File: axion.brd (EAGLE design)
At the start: 100 x 80.5 mm, 148 parts, among them IC1 3.3V, IC2 5V, Q2 12.288Mhz, U10 MIC2039, U11 WM8731, U2 Intel Edison, U4 FT232RLSSOP, U5 PCA9306D, U6 74HC4050, U7 TPA2005D1DGN, X2 ZX62R-AB-5P, X3 ST-005-G, X4 ZX62R-B-5P

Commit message: Power microSD
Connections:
- removed net N$49: JP25.4
- removed net N$51: JP25.6
- net +3V3: now also JP25.4
- net DGND: now also JP25.6
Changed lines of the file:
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@@
 <element name="U5" library="NXP_By_element14_Batch_1" package="SOIC127P600X175-8N" value="PCA9306D" x="66.7381" y="34.2527" smashed="yes" rot="MR90">
 <attribute name="MPN" value="PCA9306D,118" x="66.7381" y="34.2527" size="1.778" layer="28" rot="MR90" display="off"/>
+<attribute name="NAME" x="71.28978125" y="32.0683" size="1.016" layer="26" ratio="10" rot="SMR90"/>
+<attribute name="OC_FARNELL" value="1831194" x="66.7381" y="34.2527" size="1.778" layer="28" rot="MR90" display="off"/>
 <attribute name="OC_NEWARK" value="70R6428" x="66.7381" y="34.2527" size="1.778" layer="28" rot="MR90" display="off"/>
+<attribute name="PACKAGE" value="SOIC-8" x="66.7381" y="34.2527" size="1.778" layer="28" rot="MR90" display="off"/>
 <attribute name="SUPPLIER" value="NXP" x="66.7381" y="34.2527" size="1.778" layer="28" rot="MR90" display="off"/>
-<attribute name="OC_FARNELL" value="1831194" x="66.7381" y="34.2527" size="1.778" layer="28" rot="MR90" display="off"/>
-<attribute name="PACKAGE" value="SOIC-8" x="66.7381" y="34.2527" size="1.778" layer="28" rot="MR90" display="off"/>
-<attribute name="NAME" x="71.28978125" y="32.0683" size="1.016" layer="26" ratio="10" rot="SMR90"/>
 <attribute name="VALUE" x="70.062959375" y="31.923521875" size="0.8128" layer="28" ratio="10" rot="SMR90"/>
 </element>
@@
 </element>
 <element name="Q2" library="adafruit" package="HC49/S" value="12.288Mhz" x="35.6235" y="66.4972" rot="R90">
+<attribute name="MF" value="" x="35.6235" y="66.4972" size="1.778" layer="27" rot="R90" display="off"/>
+<attribute name="MPN" value="" x="35.6235" y="66.4972" size="1.778" layer="27" rot="R90" display="off"/>
 <attribute name="OC_FARNELL" value="1667008" x="35.6235" y="66.4972" size="1.778" layer="27" rot="R90" display="off"/>
 <attribute name="OC_NEWARK" value="unknown" x="35.6235" y="66.4972" size="1.778" layer="27" rot="R90" display="off"/>
-<attribute name="MF" value="" x="35.6235" y="66.4972" size="1.778" layer="27" rot="R90" display="off"/>
-<attribute name="MPN" value="" x="35.6235" y="66.4972" size="1.778" layer="27" rot="R90" display="off"/>
 </element>
 <element name="C32" library="resistor" package="C1608" value="22p" x="37.7825" y="60.0202" rot="MR0"/>
@@
 <vertex x="25.3992375" y="0"/>
 </polygon>
+<contactref element="JP25" pad="6"/>
+<wire x1="88.0872" y1="71.247" x2="83.8169" y2="74.3721" width="0" layer="19" extent="16-16"/>
 </signal>
 <signal name="+3V3" class="2">
@@
 <wire x1="55.963059375" y1="53.130196875" x2="55.8728" y2="53.22045625" width="0.1524" layer="1"/>
 <wire x1="55.8728" y1="53.22045625" x2="55.8728" y2="53.7783" width="0.1524" layer="1"/>
+<contactref element="JP25" pad="4"/>
+<wire x1="74.1697" y1="72.2217" x2="83.8169" y2="72.1721" width="0" layer="19" extent="16-16"/>
 </signal>
 <signal name="+5V" class="2">
@@
 <via x="84.8868" y="76.8096" extent="1-16" drill="0.3048"/>
 </signal>
-<signal name="N$49">
-<contactref element="JP25" pad="4"/>
-</signal>
-<signal name="N$51">
-<contactref element="JP25" pad="6"/>
-</signal>
 <signal name="N$50">

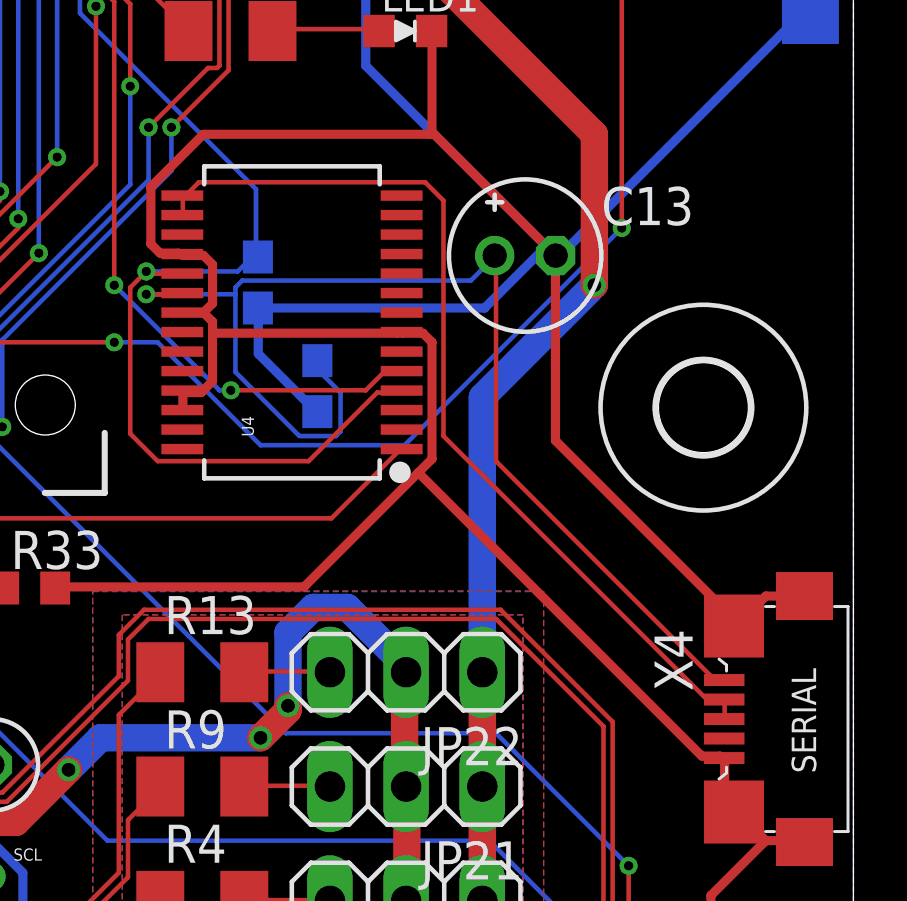
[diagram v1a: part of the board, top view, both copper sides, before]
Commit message: Disconnect between USBD{P,M} of USB-serial bridge
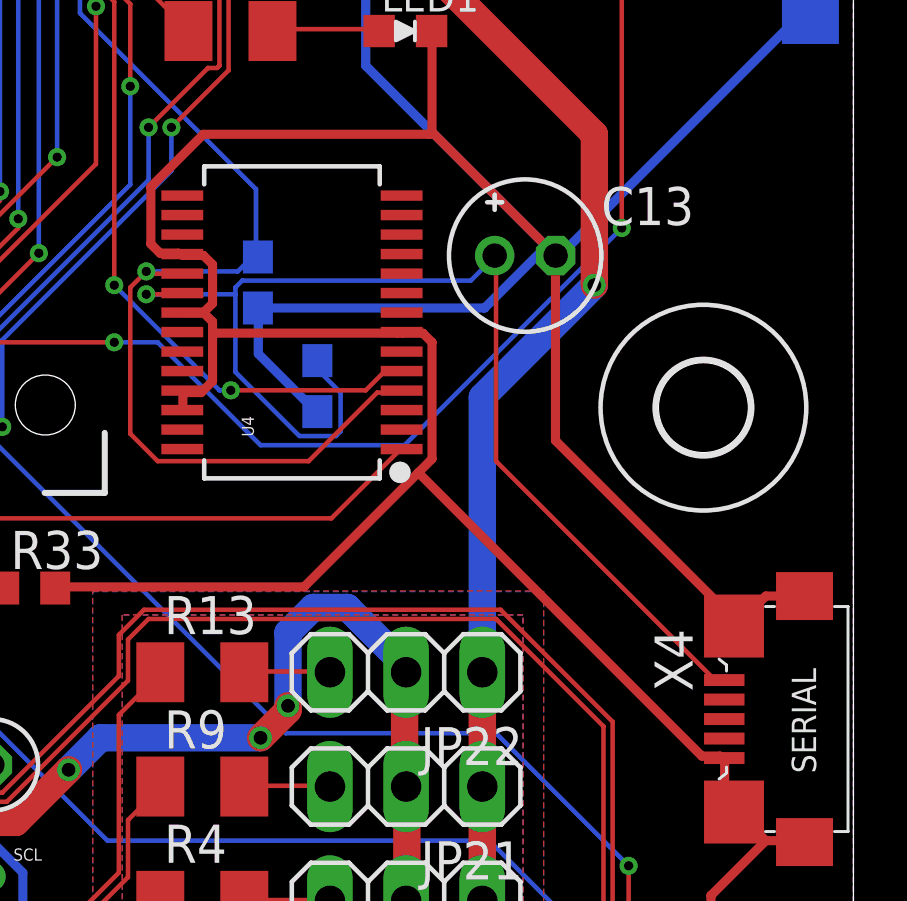
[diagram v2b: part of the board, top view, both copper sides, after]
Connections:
- new net N$49: U4.16, X4.3
- net N$8: no longer U4.16, X4.3
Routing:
- net N$8: track 31.3 -> 0.00 mm
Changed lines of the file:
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@@
 <via x="63.8556" y="50.0634" extent="1-16" drill="0.3048"/>
-</signal>
-<signal name="N$8">
-<contactref element="U4" pad="15"/>
-<contactref element="U4" pad="16"/>
-<contactref element="X4" pad="2"/>
-<contactref element="X4" pad="3"/>
-<wire x1="95.7072" y1="42.2148" x2="95.7072" y2="41.6814" width="0.1524" layer="1"/>
-<wire x1="95.7072" y1="41.6814" x2="95.695" y2="41.62" width="0.1524" layer="1"/>
-<wire x1="95.7072" y1="42.2148" x2="95.695" y2="42.27" width="0.1524" layer="1"/>
-<wire x1="77.6478" y1="59.055" x2="77.6478" y2="58.4454" width="0.1524" layer="1"/>
-<wire x1="77.6478" y1="58.4454" x2="77.6289" y2="58.4188" width="0.1524" layer="1"/>
-<wire x1="77.6478" y1="59.055" x2="77.6289" y2="59.0688" width="0.1524" layer="1"/>
-<wire x1="95.0976" y1="42.291" x2="95.631" y2="42.291" width="0.1524" layer="1"/>
-<wire x1="86.3346" y1="51.054" x2="95.0976" y2="42.291" width="0.1524" layer="1"/>
-<wire x1="86.3346" y1="58.9026" x2="86.3346" y2="51.054" width="0.1524" layer="1"/>
-<wire x1="85.725" y1="59.5122" x2="86.3346" y2="58.9026" width="0.1524" layer="1"/>
-<wire x1="78.1812" y1="59.5122" x2="85.725" y2="59.5122" width="0.1524" layer="1"/>
-<wire x1="77.724" y1="59.055" x2="78.1812" y2="59.5122" width="0.1524" layer="1"/>
-<wire x1="95.631" y1="42.291" x2="95.695" y2="42.27" width="0.1524" layer="1"/>
-<wire x1="77.724" y1="59.055" x2="77.6289" y2="59.0688" width="0.1524" layer="1"/>
 </signal>
 <signal name="I2S_RXD">
@@
 </polygon>
 </signal>
+<signal name="N$8">
+<contactref element="X4" pad="2"/>
+<contactref element="U4" pad="15"/>
+<wire x1="77.6289" y1="59.0688" x2="95.695" y2="42.27" width="0" layer="19" extent="1-1"/>
+</signal>
+<signal name="N$49">
+<contactref element="U4" pad="16"/>
+<contactref element="X4" pad="3"/>
+<wire x1="77.6289" y1="58.4188" x2="95.695" y2="41.62" width="0" layer="19" extent="1-1"/>
+</signal>
 </signals>

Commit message: Fix the order of {T,R}XD of serial
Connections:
- net UART_RXD: now also U4.1; no longer U4.5
- net UART_TXD: now also U4.5; no longer U4.1
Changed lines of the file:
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@@
 <signal name="UART_TXD">
 <contactref element="U2" pad="27"/>
-<contactref element="U4" pad="1"/>
 <wire x1="61.1124" y1="50.4444" x2="61.1124" y2="51.1302" width="0.1524" layer="1"/>
 <wire x1="63.246" y1="48.3108" x2="61.1124" y2="50.4444" width="0.1524" layer="1"/>
@@
 <wire x1="84.8868" y1="50.5968" x2="82.6008" y2="48.3108" width="0.1524" layer="1"/>
 <wire x1="61.1124" y1="51.1302" x2="61.0728" y2="51.1383" width="0.1524" layer="1"/>
-<wire x1="84.8868" y1="50.5968" x2="84.9409" y2="50.6188" width="0.1524" layer="1"/>
+<contactref element="U4" pad="5"/>
+<wire x1="84.8868" y1="50.5968" x2="84.9409" y2="53.2188" width="0" layer="19" extent="1-1"/>
 </signal>
 <signal name="UART_RXD">
 <contactref element="U2" pad="22"/>
-<contactref element="U4" pad="5"/>
 <wire x1="59.8932" y1="54.864" x2="59.8932" y2="53.7972" width="0.1524" layer="1"/>
 <wire x1="59.8932" y1="56.9976" x2="59.8932" y2="54.864" width="0.1524" layer="16"/>
@@
 <wire x1="84.8868" y1="53.1876" x2="84.3534" y2="53.1876" width="0.1524" layer="1"/>
 <wire x1="59.8932" y1="53.7972" x2="59.8728" y2="53.7783" width="0.1524" layer="1"/>
-<wire x1="84.8868" y1="53.1876" x2="84.9409" y2="53.2188" width="0.1524" layer="1"/>
 <via x="59.8932" y="54.864" extent="1-16" drill="0.3048"/>
 <via x="62.4078" y="59.2836" extent="1-16" drill="0.3048"/>
 <via x="75.3618" y="56.0832" extent="1-16" drill="0.3048"/>
 <via x="79.248" y="52.578" extent="1-16" drill="0.3048"/>
+<contactref element="U4" pad="1"/>
+<wire x1="83.7438" y1="52.578" x2="84.9409" y2="50.6188" width="0" layer="19" extent="1-1"/>
 </signal>
 <signal name="2P0">

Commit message: Fix the order of USBD{P,M} od OTG USB
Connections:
- net USB_DN: now also X2.2; no longer X2.3
- net USB_DP: now also X2.3; no longer X2.2
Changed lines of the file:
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@@
 <signal name="USB_DP">
 <contactref element="U2" pad="16"/>
-<contactref element="X2" pad="2"/>
 <wire x1="58.674" y1="54.4068" x2="58.674" y2="53.7972" width="0.1524" layer="1"/>
 <wire x1="59.6646" y1="55.3974" x2="58.674" y2="54.4068" width="0.1524" layer="1"/>
@@
 <wire x1="95.4786" y1="27.1272" x2="94.4118" y2="27.1272" width="0.1524" layer="1"/>
 <wire x1="58.674" y1="53.7972" x2="58.6728" y2="53.7783" width="0.1524" layer="1"/>
-<wire x1="95.4786" y1="27.1272" x2="95.4913" y2="27.0542" width="0.1524" layer="1"/>
 <via x="68.0466" y="56.6166" extent="1-16" drill="0.3048"/>
 <via x="92.5068" y="36.7284" extent="1-16" drill="0.3048"/>
+<contactref element="X2" pad="3"/>
+<wire x1="95.4786" y1="27.1272" x2="95.4913" y2="26.4042" width="0" layer="19" extent="1-1"/>
 </signal>
 <signal name="USB_DN">
 <contactref element="U2" pad="18"/>
-<contactref element="X2" pad="3"/>
 <wire x1="59.055" y1="53.0352" x2="59.055" y2="53.721" width="0.1524" layer="1"/>
 <wire x1="58.7502" y1="52.7304" x2="59.055" y2="53.0352" width="0.1524" layer="1"/>
@@
 <wire x1="95.4786" y1="26.4414" x2="94.6404" y2="26.4414" width="0.1524" layer="1"/>
 <wire x1="59.055" y1="53.721" x2="59.0728" y2="53.7783" width="0.1524" layer="1"/>
-<wire x1="95.4786" y1="26.4414" x2="95.4913" y2="26.4042" width="0.1524" layer="1"/>
 <via x="58.7502" y="52.7304" extent="1-16" drill="0.3048"/>
 <via x="68.961" y="41.2242" extent="1-16" drill="0.3048"/>
+<contactref element="X2" pad="2"/>
+<wire x1="95.4786" y1="26.4414" x2="95.4913" y2="27.0542" width="0" layer="19" extent="1-1"/>
 </signal>
 <signal name="USB_VBUS">

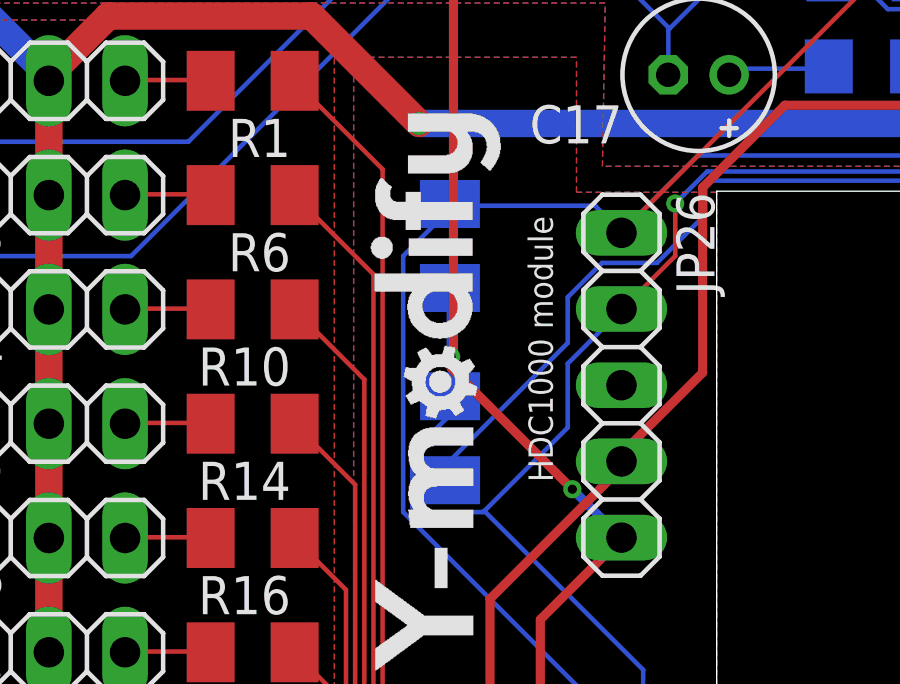
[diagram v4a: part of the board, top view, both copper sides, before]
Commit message: Remove 10k pullup of I2C
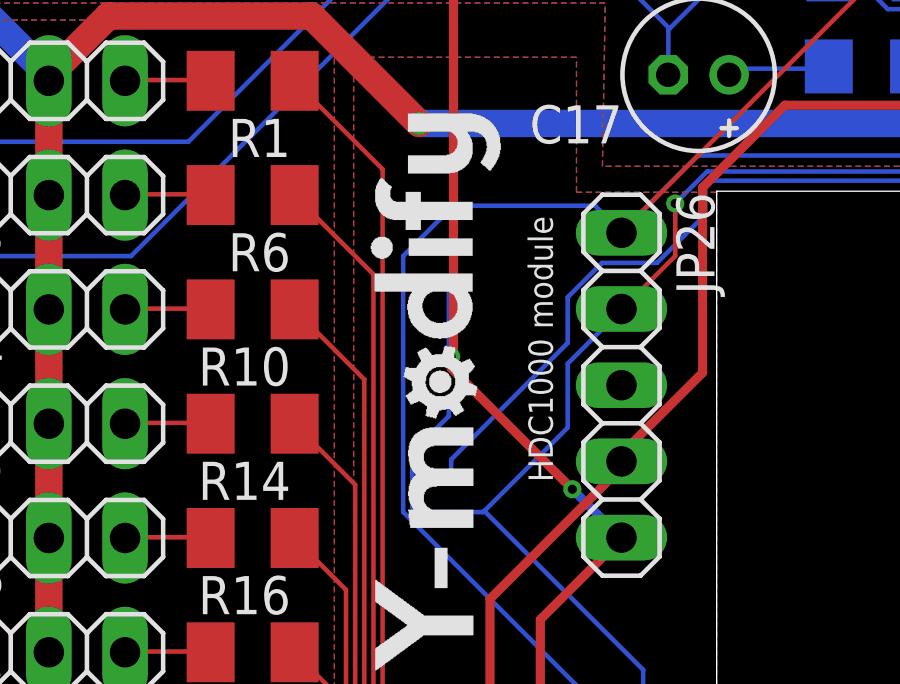
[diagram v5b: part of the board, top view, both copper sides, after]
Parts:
- removed R30, R36: 10k, resistor:M1206
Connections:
- net +3V3: no longer R30.2
- net 3V3SCL: no longer R36.1
- net 3V3SDA: no longer R30.1
- net N$10: no longer R36.2
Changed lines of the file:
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@@
 <element name="C26" library="resistor" package="E2-5" value="10u" x="25.23" y="48.78" rot="R180"/>
 <element name="R26" library="resistor" package="R0603" value="47k" x="16.09" y="55.23" rot="MR90"/>
-<element name="R30" library="resistor" package="M1206" value="10k" x="28.60801875" y="37.67328125" rot="MR270"/>
-<element name="R36" library="resistor" package="M1206" value="10k" x="28.615640625" y="31.264859375" rot="MR270"/>
 <element name="JP27" library="pinhead" package="1X02" value="PCTRL" x="61.495940625" y="78.04911875" smashed="yes" rot="R180">
 <attribute name="NAME" x="64.112140625" y="76.22031875" size="1.27" layer="25" ratio="10" rot="R180"/>
@@
 <contactref element="U11" pad="1"/>
 <contactref element="U11" pad="27"/>
-<contactref element="R30" pad="2"/>
 <contactref element="R37" pad="2"/>
 <contactref element="TP6" pad="TP"/>
@@
 <wire x1="32.6898" y1="29.5656" x2="28.6512" y2="33.6042" width="0.3048" layer="1"/>
 <wire x1="34.29" y1="27.9654" x2="32.6898" y2="29.5656" width="0.3048" layer="16"/>
-<wire x1="28.6512" y1="36.2712" x2="28.60801875" y2="36.27328125" width="0.3048" layer="16"/>
 <wire x1="34.29" y1="27.9654" x2="34.3281" y2="27.9527" width="0.3048" layer="16"/>
 <wire x1="31.623" y1="25.2222" x2="31.623" y2="19.2024" width="0.3048" layer="1"/>
@@
 <contactref element="JP26" pad="1"/>
 <contactref element="U11" pad="23"/>
-<contactref element="R30" pad="1"/>
 <wire x1="63.7032" y1="8.382" x2="65.2272" y2="8.382" width="0.1524" layer="1"/>
 <wire x1="63.7032" y1="35.7378" x2="63.7032" y2="8.382" width="0.1524" layer="16"/>
@@
 <wire x1="33.4518" y1="39.0144" x2="28.6512" y2="39.0144" width="0.1524" layer="16"/>
 <wire x1="34.29" y1="38.1762" x2="33.4518" y2="39.0144" width="0.1524" layer="16"/>
-<wire x1="28.6512" y1="39.0144" x2="28.60801875" y2="39.07328125" width="0.1524" layer="16"/>
 <wire x1="34.29" y1="38.1762" x2="34.3281" y2="38.1127" width="0.1524" layer="16"/>
 <wire x1="32.8422" y1="23.0124" x2="32.8422" y2="15.4686" width="0.1524" layer="16"/>
@@
 <wire x1="27.051" y1="37.338" x2="27.051" y2="28.8036" width="0.1524" layer="16"/>
 <wire x1="28.6512" y1="38.9382" x2="27.051" y2="37.338" width="0.1524" layer="16"/>
-<wire x1="28.6512" y1="38.9382" x2="28.60801875" y2="39.07328125" width="0.1524" layer="16"/>
 <wire x1="63.0936" y1="38.5572" x2="64.77" y2="36.8808" width="0.1524" layer="16"/>
 <wire x1="63.0936" y1="39.3954" x2="63.0936" y2="38.5572" width="0.1524" layer="1"/>
@@
 <via x="63.0936" y="38.5572" extent="1-16" drill="0.3048"/>
 <via x="61.7982" y="40.6908" extent="1-16" drill="0.3048"/>
+<wire x1="28.6512" y1="38.9382" x2="28.6512" y2="39.0144" width="0" layer="19" extent="16-16"/>
 </signal>
 <signal name="3V3SCL">
@@
 <contactref element="JP23" pad="1"/>
 <contactref element="JP26" pad="2"/>
-<contactref element="R36" pad="1"/>
 <wire x1="34.29" y1="15.3924" x2="33.8328" y2="15.3924" width="0.1524" layer="1"/>
 <wire x1="35.3568" y1="14.3256" x2="34.29" y2="15.3924" width="0.1524" layer="1"/>
@@
 <wire x1="32.5374" y1="33.7566" x2="32.5374" y2="31.623" width="0.1524" layer="16"/>
 <wire x1="34.29" y1="35.5092" x2="32.5374" y2="33.7566" width="0.1524" layer="16"/>
-<wire x1="28.575" y1="32.6136" x2="28.615640625" y2="32.664859375" width="0.1524" layer="16"/>
 <wire x1="34.29" y1="35.5092" x2="34.3281" y2="35.5727" width="0.1524" layer="16"/>
 <wire x1="35.052" y1="23.5458" x2="35.052" y2="4.1148" width="0.1524" layer="16"/>
@@
 <contactref element="C14" pad="1"/>
 <contactref element="U5" pad="7"/>
-<contactref element="R36" pad="2"/>
 <wire x1="64.9224" y1="30.099" x2="64.9224" y2="28.575" width="0.1524" layer="16"/>
 <wire x1="64.3128" y1="30.7086" x2="64.9224" y2="30.099" width="0.1524" layer="16"/>
@@
 <wire x1="65.532" y1="35.9664" x2="65.532" y2="37.6428" width="0.1524" layer="16"/>
 <wire x1="66.1035" y1="35.3949" x2="65.532" y2="35.9664" width="0.1524" layer="16"/>
-<wire x1="28.6512" y1="29.8704" x2="28.615640625" y2="29.864859375" width="0.1524" layer="16"/>
 <wire x1="68.7324" y1="37.1094" x2="68.7324" y2="40.0812" width="0.1524" layer="16"/>
 <wire x1="68.58" y1="36.957" x2="68.7324" y2="37.1094" width="0.1524" layer="16"/>

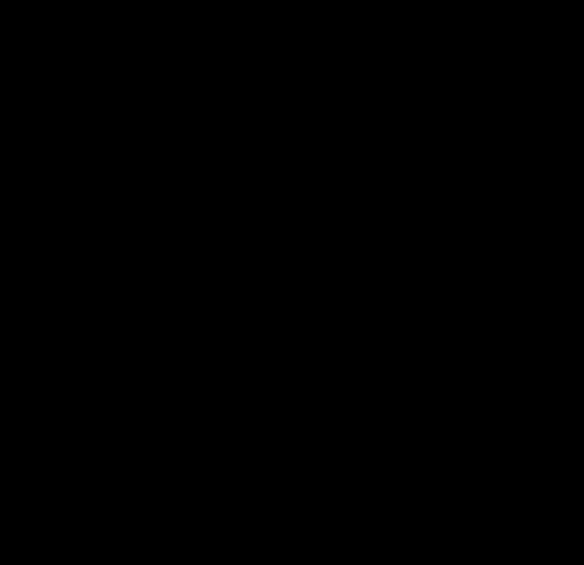
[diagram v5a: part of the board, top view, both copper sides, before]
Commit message: Add 820 pullup to 1v8 side of I2c
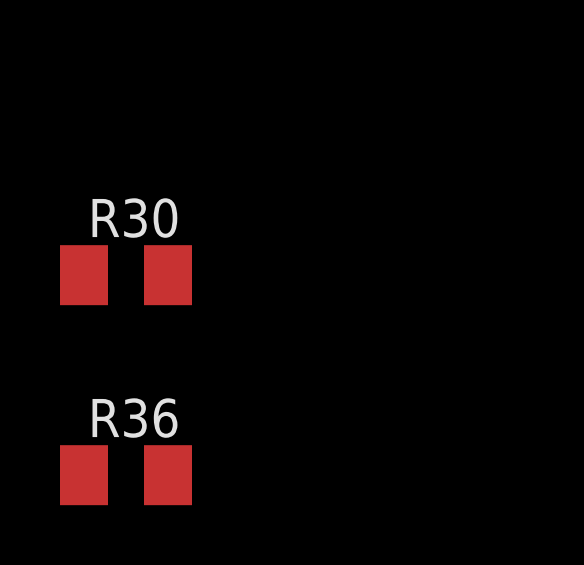
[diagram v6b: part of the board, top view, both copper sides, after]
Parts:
- added R30, R36: 820, resistor:M1206
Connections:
- net +1V8: now also R30.2, R36.2
- net 1V8SCL: now also R30.1
- net 1V8SDA: now also R36.1
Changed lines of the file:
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@@
 </element>
 <element name="X4" library="hirose-zx" package="ZX62R-B-5P" value="ZX62R-B-5P" x="98.37" y="41.62" rot="R180"/>
+<element name="R30" library="resistor" package="M1206" value="820" x="-9.937" y="-14.179"/>
+<element name="R36" library="resistor" package="M1206" value="820" x="-9.937" y="-20.846"/>
 </elements>
 <signals>
@@
 <via x="56.4642" y="54.864" extent="1-16" drill="0.3048"/>
 <via x="63.4746" y="42.4434" extent="1-16" drill="0.3048"/>
+<contactref element="R36" pad="2"/>
+<contactref element="R30" pad="2"/>
+<wire x1="-8.537" y1="-14.179" x2="49.3776" y2="43.434" width="0" layer="19" extent="1-1"/>
+<wire x1="-8.537" y1="-20.846" x2="-8.537" y2="-14.179" width="0" layer="19" extent="1-1"/>
 </signal>
 <signal name="UART_TXD">
@@
 <via x="64.6176" y="50.0634" extent="1-16" drill="0.3048"/>
 <via x="69.2658" y="35.6616" extent="1-16" drill="0.3048"/>
+<contactref element="R36" pad="1"/>
+<wire x1="-11.337" y1="-20.846" x2="64.8331" y2="31.6619" width="0" layer="19" extent="1-16"/>
 </signal>
 <signal name="1V8SCL">
@@
 <wire x1="70.9422" y1="36.576" x2="71.241921875" y2="36.3728" width="0.1524" layer="16"/>
 <via x="63.8556" y="50.0634" extent="1-16" drill="0.3048"/>
+<contactref element="R30" pad="1"/>
+<wire x1="-11.337" y1="-14.179" x2="66.1031" y2="31.6619" width="0" layer="19" extent="1-16"/>
 </signal>
 <signal name="I2S_RXD">
